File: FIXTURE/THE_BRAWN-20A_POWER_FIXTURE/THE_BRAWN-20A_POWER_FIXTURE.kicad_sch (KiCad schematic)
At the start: 70 parts, among them J1 Pins_2.54_1x3, J10 Pins_2.54_1x2, J2 Pins_2.54_1x3, J3 Pins_2.54_1x4, J4 Pins_2.54_1x3, J5 Pins_2.54_1x2, J6 Pins_2.54_1x3, J7 Pins_2.54_1x4, J8 Pins_2.54_1x3, J9 Pins_2.54_1x3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

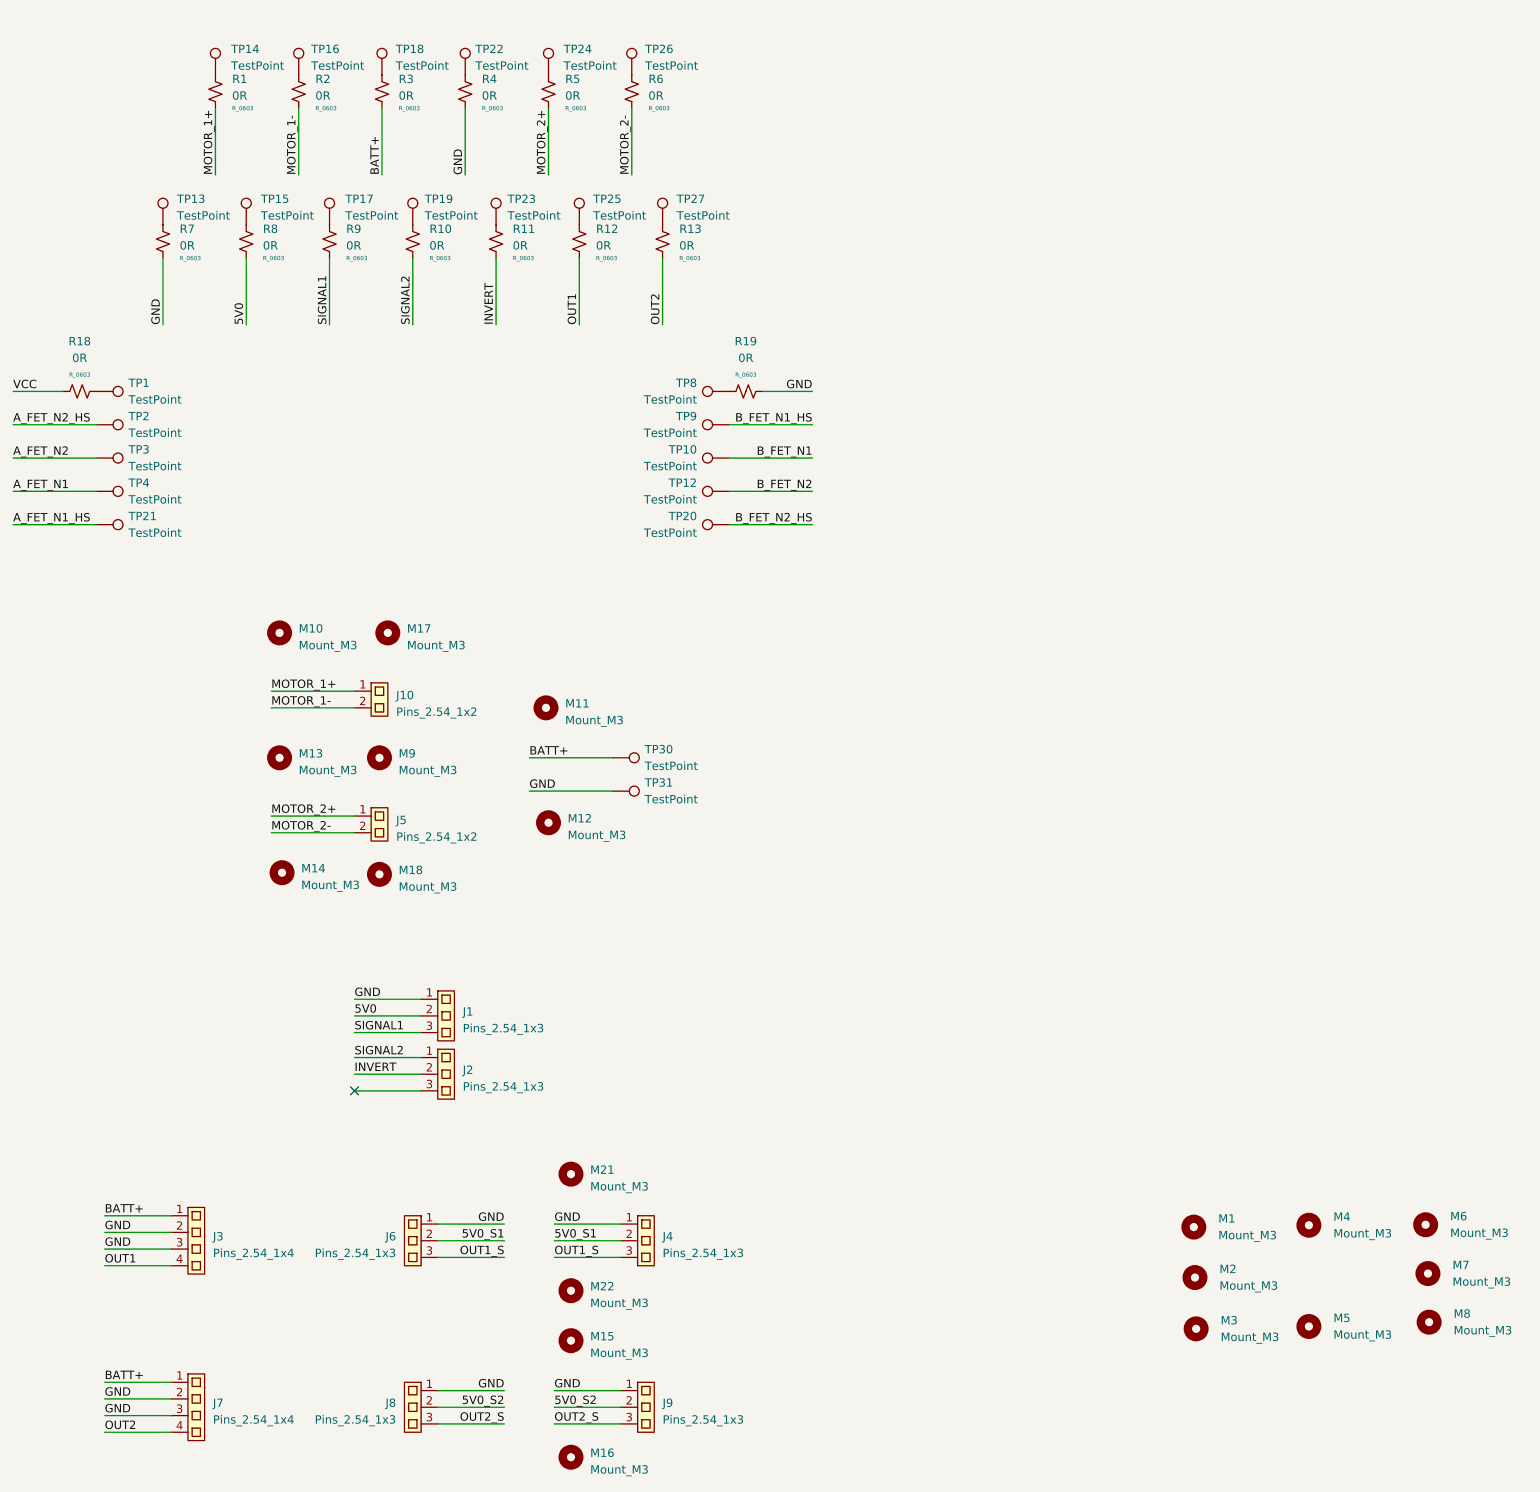
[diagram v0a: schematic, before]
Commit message: Finish Tracking Power Fixture PCB
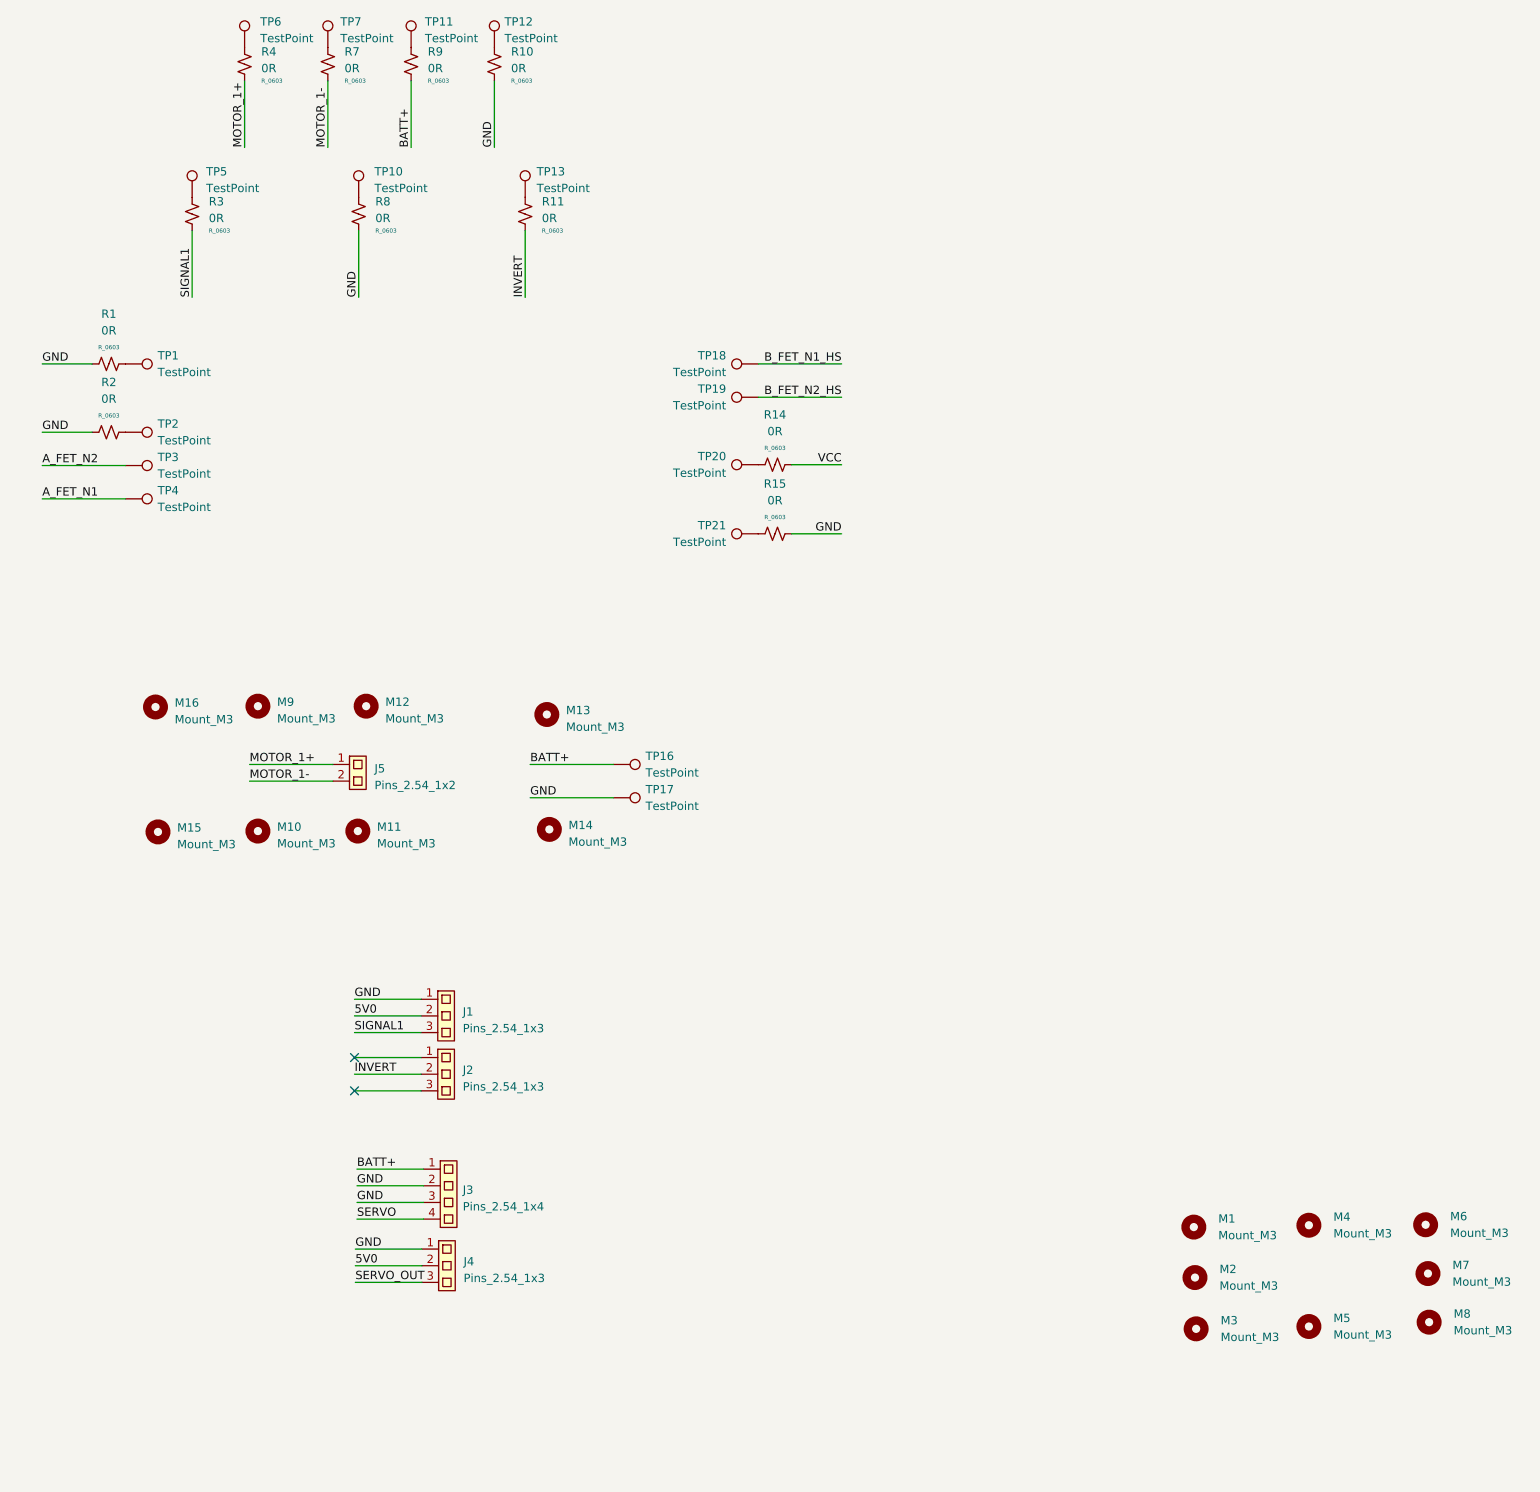
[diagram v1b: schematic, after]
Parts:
- removed J10: Pins_2.54_1x2, .J_Connector:Pins-2.54-1x2, symbol .J_Connector:Pins_2.54_1x2
- removed J6, J8, J9: Pins_2.54_1x3, .J_Connector:Pins-2.54-1x3, symbol .J_Connector:Pins_2.54_1x3
- removed J7: Pins_2.54_1x4, .J_Connector:Pins-2.54-1x4, symbol .J_Connector:Pins_2.54_1x4
- removed M17, M18, M21, M22: Mount_M3, .M_Mechanical:Mount_M3, symbol .M_Mechanical:Mount_M3
- removed R12, R13, R18, R19, R5, R6: 0R, .R_Resistor:R_0603, symbol .R_Resistor:R_0603
- removed TP14, TP15, TP22, TP23, TP24, TP25, TP26, TP27, TP30, TP31, TP8, TP9: TestPoint, TestPoint:TestPoint_THTPad_D3.0mm_Drill1.5mm, symbol Connector:TestPoint
- added R14, R15: 0R, .R_Resistor:R_0603, symbol .R_Resistor:R_0603
- added TP11, TP5, TP6, TP7: TestPoint, TestPoint:TestPoint_THTPad_D3.0mm_Drill1.5mm, symbol Connector:TestPoint
- J3: footprint .J_Connector:Pins-2.54-1x4 -> J_Connector:Pins-2.54-1x4
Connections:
- net 5V0_S1 is gone; now on net 5V0: J4.2
- net B_FET_N1 is gone; now on an unnamed net: TP10.1
- net B_FET_N2 is gone; now on an unnamed net: TP12.1
- net MOTOR_2+ is gone; now on net MOTOR_1+: J5.1
- net MOTOR_2- is gone; now on net MOTOR_1-: J5.2
- net 5V0: no longer R8.2
- net BATT+: now also R9.2, TP16.1; no longer R3.2
- net B_FET_N1_HS: now also TP18.1
- net B_FET_N2_HS: now also TP19.1; no longer TP20.1
- net GND: now also R1.1, R10.2, R2.1, R8.2, TP17.1, R15.2; no longer R4.2, R7.2
- net MOTOR_1+: now also R4.2; no longer R1.2
- net MOTOR_1-: now also R7.2; no longer R2.2
- net SIGNAL1: now also R3.2; no longer R9.2
- net VCC: now also R14.2
- net at R9.1: now also TP11.1; no longer TP17.1
- net at R4.1: now also TP6.1
- net at R7.1: now also TP7.1; no longer TP13.1
- net at R3.1: now also TP5.1; no longer TP18.1
- net at R11.1: now also TP13.1
- net at TP1.1: now also R1.2
- net at R10.1: no longer TP19.1
- net A_FET_N1_HS: no longer names the net of TP21.1
- net A_FET_N1_HS: now also R15.1
- net A_FET_N2_HS: no longer names the net of TP2.1
- net A_FET_N2_HS: now also R2.2
- net OUT1 renamed SERVO
- net OUT1_S renamed SERVO_OUT
- net SIGNAL2: no longer names the net of J2.1
- net SIGNAL2: no longer R10.2
- new net: R14.1, TP20.1
- no-connect marks 1 -> 2
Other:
- title: THE BRAWN - 20A POWER FIXTURE -> THE BRAWN - 20A LOGIC FIXTURE
